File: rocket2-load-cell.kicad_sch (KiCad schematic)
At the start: 34 parts, among them J1 SWD, J2 Screw_Terminal_01x02, Q1 MMBT4403, U2 STM32F103C8Tx, U3 AMS1117-3.3, U4 HX711, Y1 16MHz

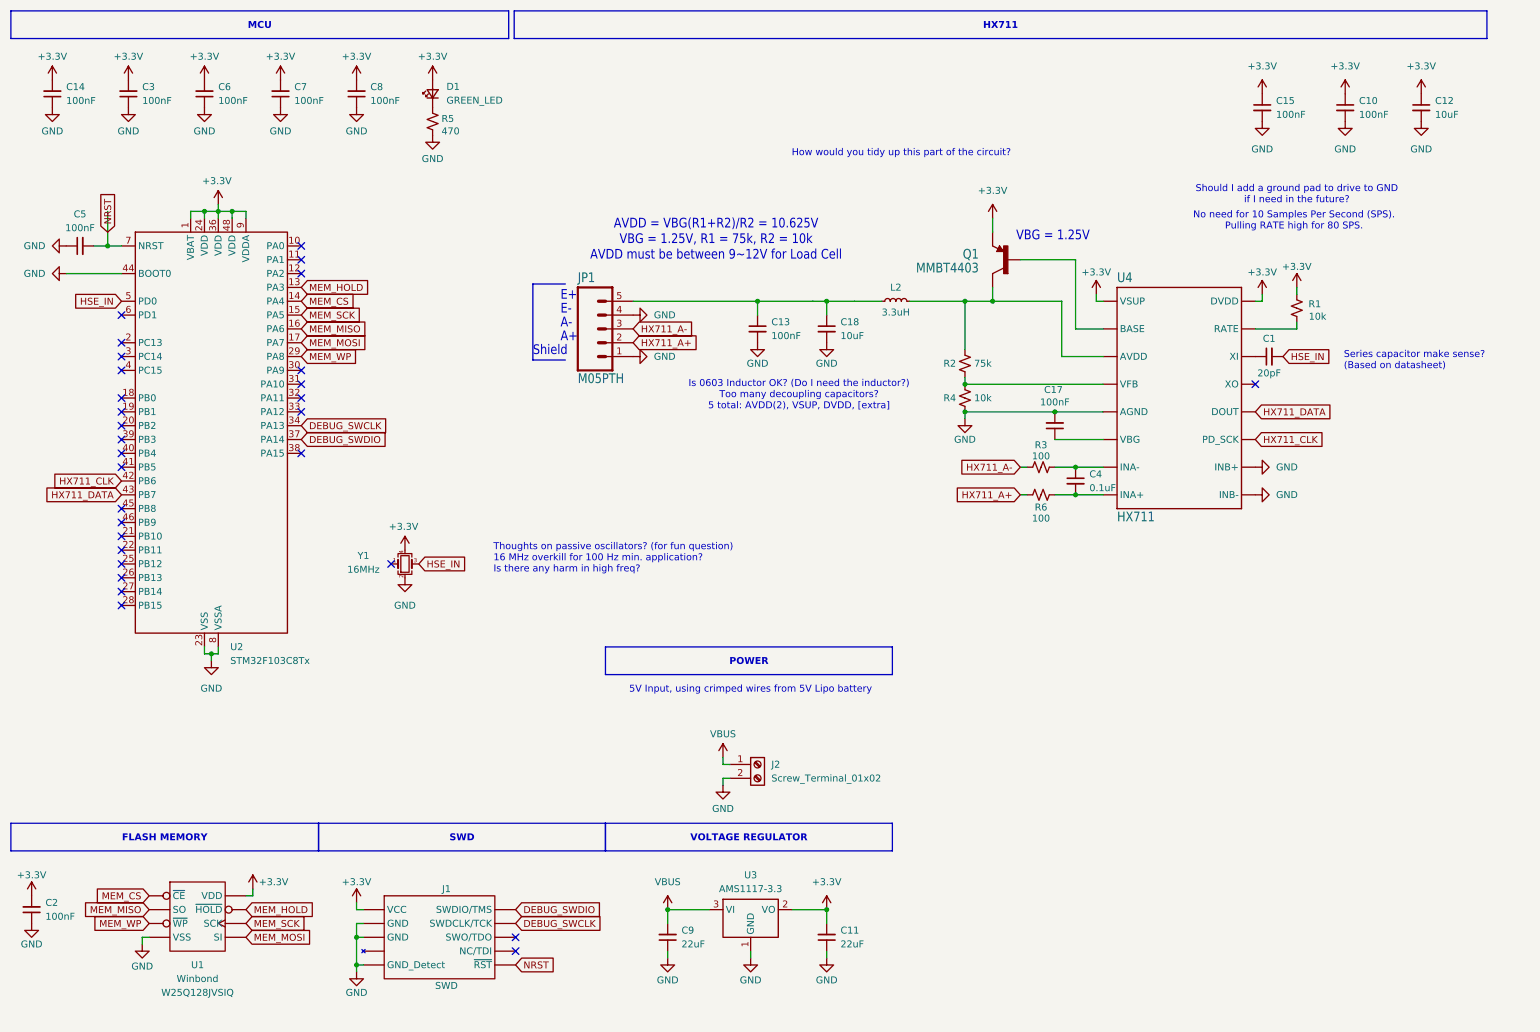
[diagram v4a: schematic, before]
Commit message: Resolved comments. Need new amplifier for faster sampling.
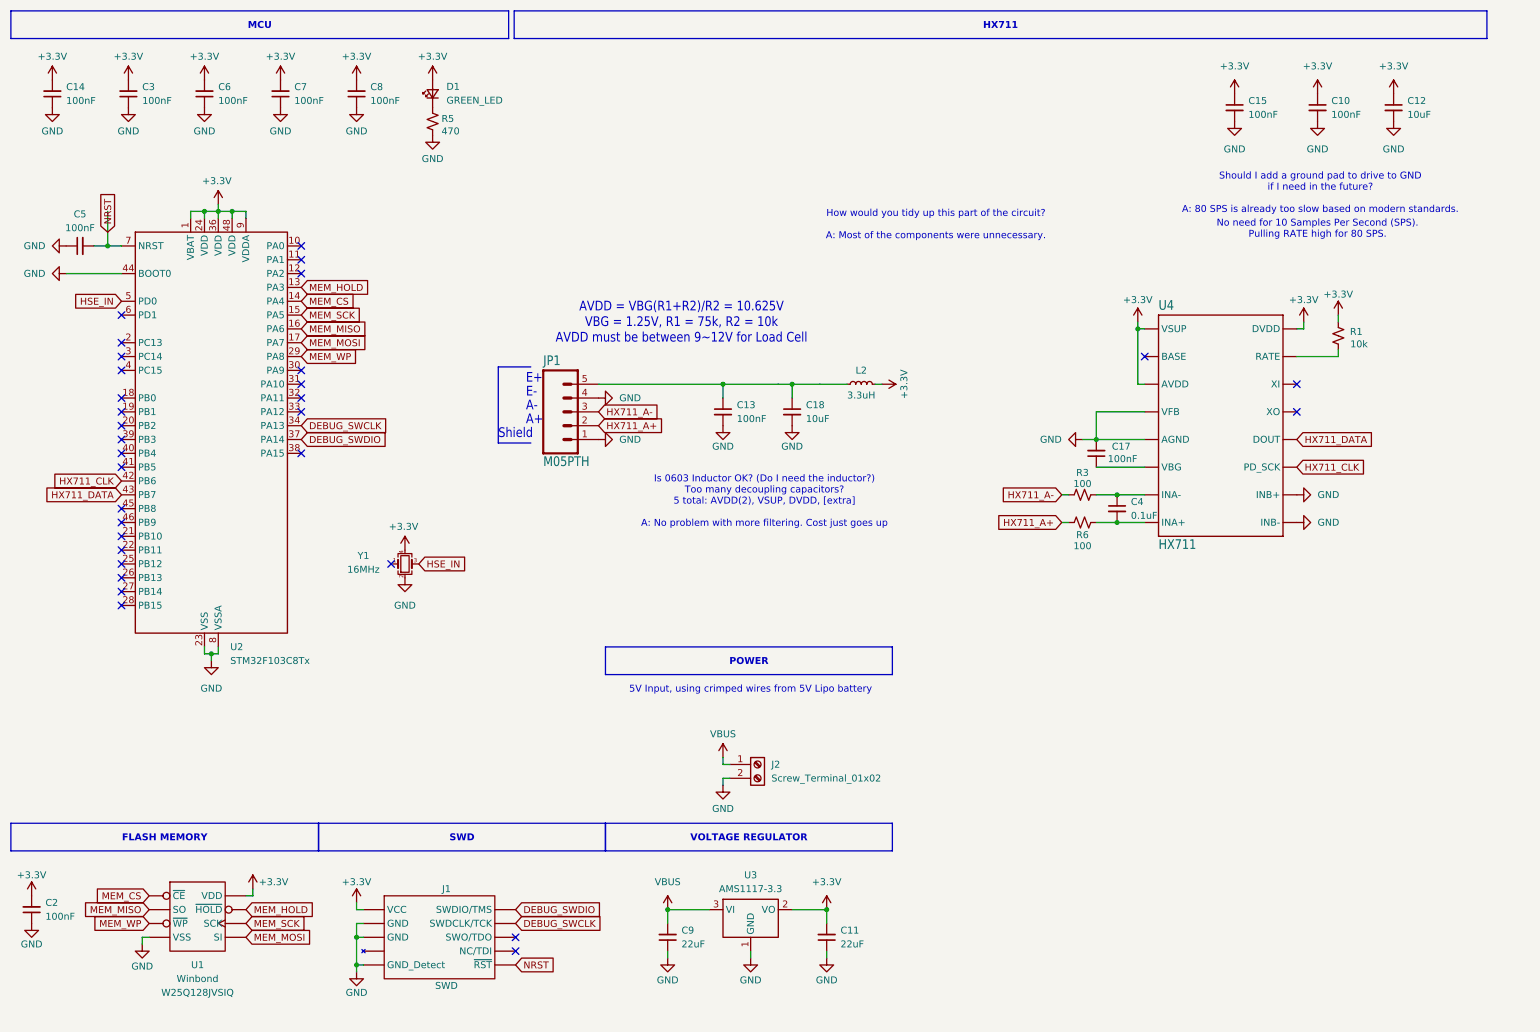
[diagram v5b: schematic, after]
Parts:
- removed C1: 20pF, Capacitor_SMD:C_0603_1608Metric, symbol Device:C_Small
- removed Q1: MMBT4403, symbol SparkFun_HX711_Load_Cell-eagle-import:TRANSISTOR_PNPMMBT4403
- removed R2: 75k, Resistor_SMD:R_0603_1608Metric, symbol Device:R_Small_US
- removed R4: 10k, Resistor_SMD:R_0603_1608Metric, symbol Device:R_Small_US
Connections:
- net +3.3V: now also L2.2, U4.3 (AVDD)
- net GND: now also U4.4 (VFB)
- no-connect marks 30 -> 32
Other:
- note added: "How would you tidy up this part of the circuit? A: Most of the components were unnecessary."
- note added: "Is 0603 Inductor OK? (Do I need the inductor?) Too many decoupling capacitors? 5 total: AVDD(2), VSUP, DVDD, [extra] A: No problem with more filtering. Cost just goes up"
- note added: "Should I add a ground pad to drive to GND if I need in the future? A: 80 SPS is already too slow based on modern standards."
- note removed: "How would you tidy up this part of the circuit?"
- note removed: "Is 0603 Inductor OK? (Do I need the inductor?) Too many decoupling capacitors? 5 total: AVDD(2), VSUP, DVDD, [extra]"
- note removed: "Series capacitor make sense? (Based on datasheet)"
- note removed: "Should I add a ground pad to drive to GND if I need in the future?"
- note removed: "Thoughts on passive oscillators? (for fun question) 16 MHz overkill for 100 Hz min. application? Is there any harm in high freq?"
- note removed: "VBG = 1.25V"
- moved on the sheet: C10, C12, C13, C15, C17, C18, C4, JP1, L2, R1, R3, R6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

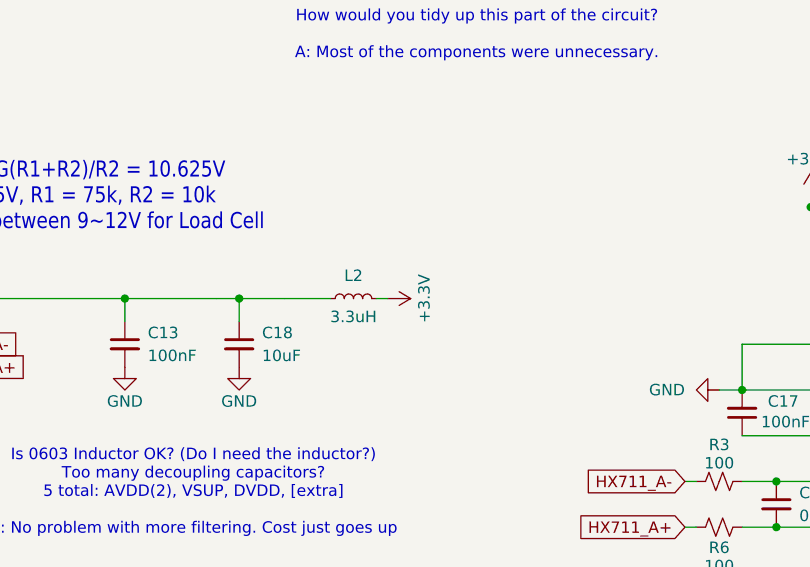
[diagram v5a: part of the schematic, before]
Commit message: Load cell E+ +3.3 -> +5V
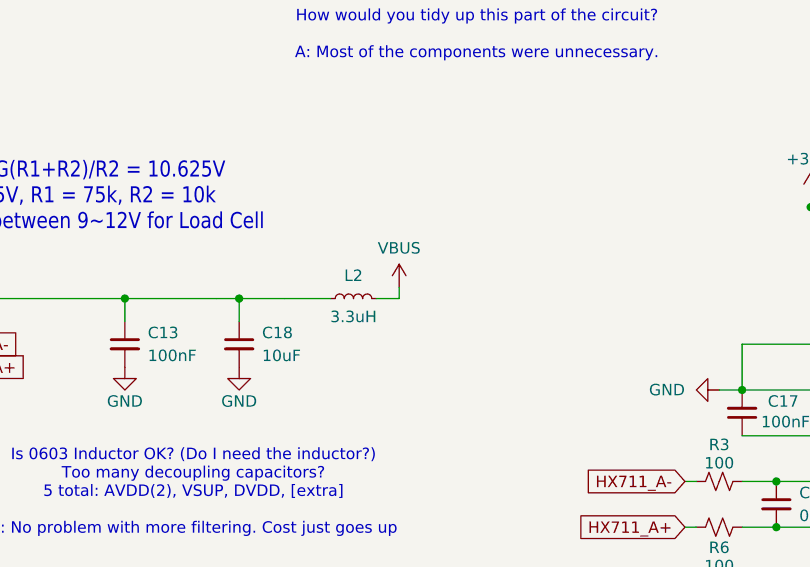
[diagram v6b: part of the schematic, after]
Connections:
- net +3.3V: no longer L2.2
- net VBUS: now also L2.2
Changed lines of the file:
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@@
 	(wire
 		(pts
-			(xy 172.72 81.28) (xy 171.45 81.28)
+			(xy 171.45 81.28) (xy 173.99 81.28)
 		)
 		(stroke
@@
 	(wire
 		(pts
+			(xy 173.99 80.01) (xy 173.99 81.28)
+		)
+		(stroke
+			(width 0)
+			(type default)
+		)
+	)
+	(wire
+		(pts
 			(xy 49.53 130.81) (xy 49.53 132.08)
 		)
@@
 	)
 	(symbol
+		(lib_id "power:VBUS")
+		(at 173.99 80.01 0)
+		(unit 1)
+		(exclude_from_sim no)
+		(in_bom yes)
+		(on_board yes)
+		(dnp no)
+		(property "Reference" "#PWR030"
+			(at 173.99 83.82 0)
+			(effects
+				(font
+					(size 1.27 1.27)
+				)
+				(hide yes)
+			)
+		)
+		(property "Value" "VBUS"
+			(at 173.99 75.692 0)
+			(effects
+				(font
+					(size 1.27 1.27)
+				)
+			)
+		)
+		(property "Footprint" ""
+			(at 173.99 80.01 0)
+			(effects
+				(font
+					(size 1.27 1.27)
+				)
+				(hide yes)
+			)
+		)
+		(property "Datasheet" ""
+			(at 173.99 80.01 0)
+			(effects
+				(font
+					(size 1.27 1.27)
+				)
+				(hide yes)
+			)
+		)
+		(property "Description" "Power symbol creates a global label with name \"VBUS\""
+			(at 173.99 80.01 0)
+			(effects
+				(font
+					(size 1.27 1.27)
+				)
+				(hide yes)
+			)
+		)
+		(pin "1"
+		)
+		(instances
+			(project "rocket2-load-cell"
+				(path "/d1f04dc8-a56c-4379-8ad0-2916e7244fc3"
+					(reference "#PWR030")
+					(unit 1)
+				)
+			)
+		)
+	)
+	(symbol
 		(lib_id "power:GND")
 		(at 266.7 33.02 0)
@@
 					(unit 1)
 				)
-			)
-		)
-	)
-	(symbol
-		(lib_id "power:+3.3V")
-		(at 172.72 81.28 270)
-		(unit 1)
-		(exclude_from_sim no)
-		(in_bom yes)
-		(on_board yes)
-		(dnp no)
-		(property "Reference" "#PWR030"
-			(at 168.91 81.28 0)
-			(effects
-				(font
-					(size 1.27 1.27)
-				)
-				(hide yes)
-			)
-		)
-		(property "Value" "+3.3V"
-			(at 176.784 81.28 0)
-			(effects
-				(font
-					(size 1.27 1.27)
-				)
-			)
-		)
-		(property "Footprint" ""
-			(at 172.72 81.28 0)
-			(effects
-				(font
-					(size 1.27 1.27)
-				)
-				(hide yes)
-			)
-		)
-		(property "Datasheet" ""
-			(at 172.72 81.28 0)
-			(effects
-				(font
-					(size 1.27 1.27)
-				)
-				(hide yes)
-			)
-		)
-		(property "Description" "Power symbol creates a global label with name \"+3.3V\""
-			(at 172.72 81.28 0)
-			(effects
-				(font
-					(size 1.27 1.27)
-				)
-				(hide yes)
-			)
-		)
-		(pin "1"
-		)
-		(instances
-			(project "rocket2-load-cell"
-				(path "/d1f04dc8-a56c-4379-8ad0-2916e7244fc3"
-					(reference "#PWR030")
-					(unit 1)
-				)

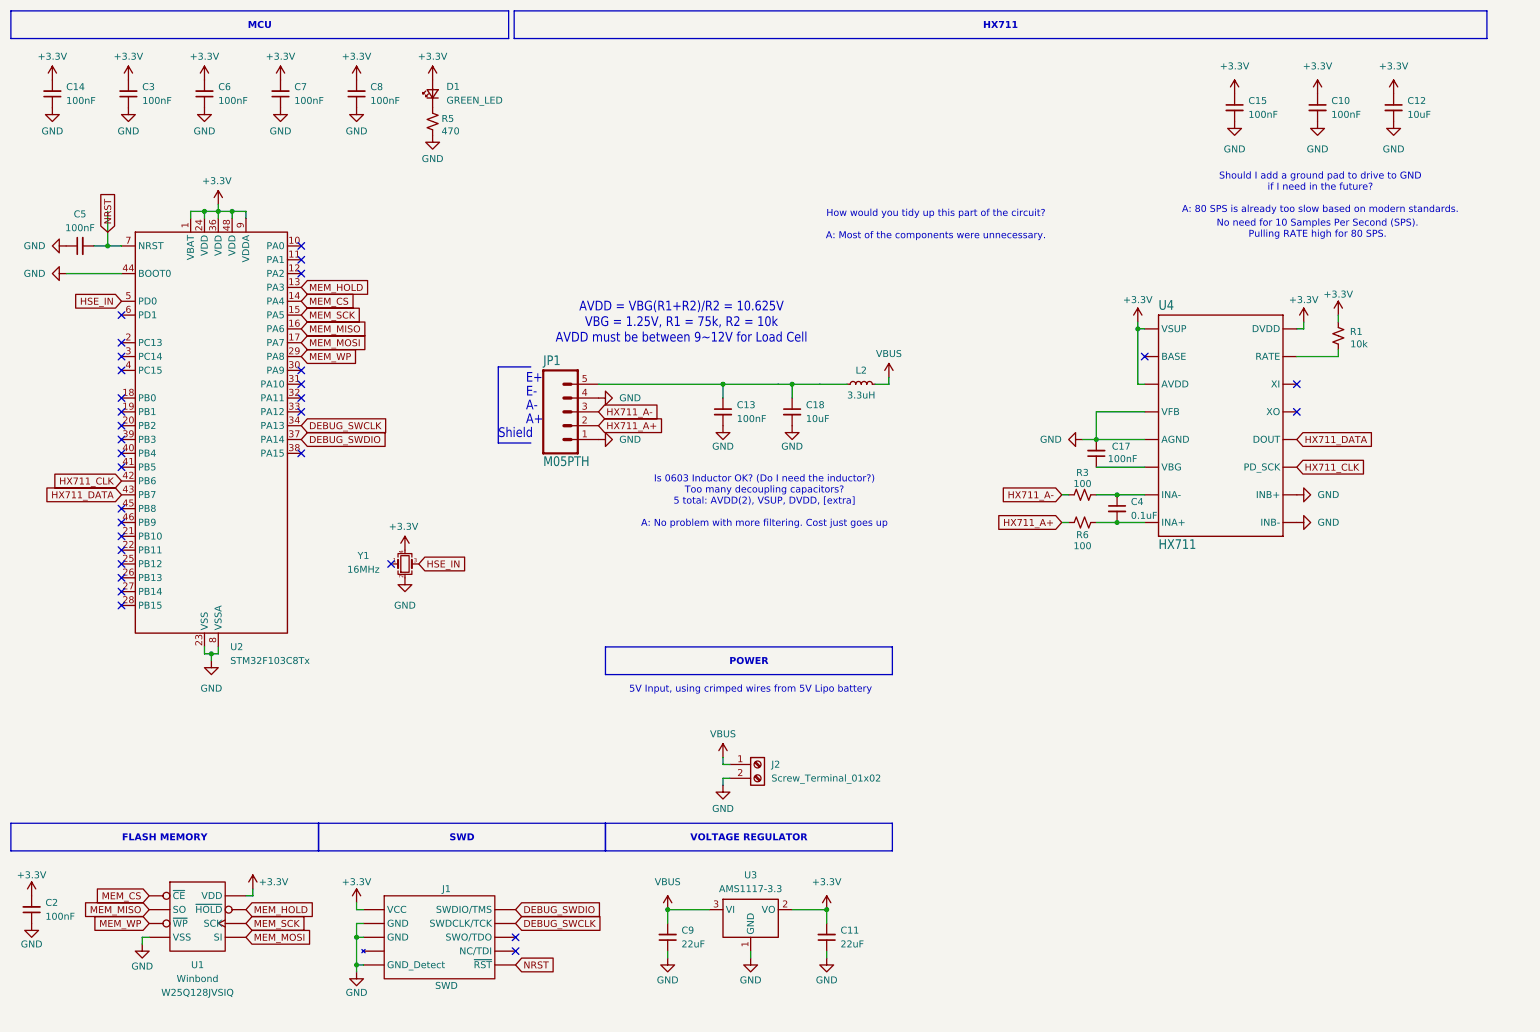
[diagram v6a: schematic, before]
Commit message: added working arduino code as well as testread.py(nonop)
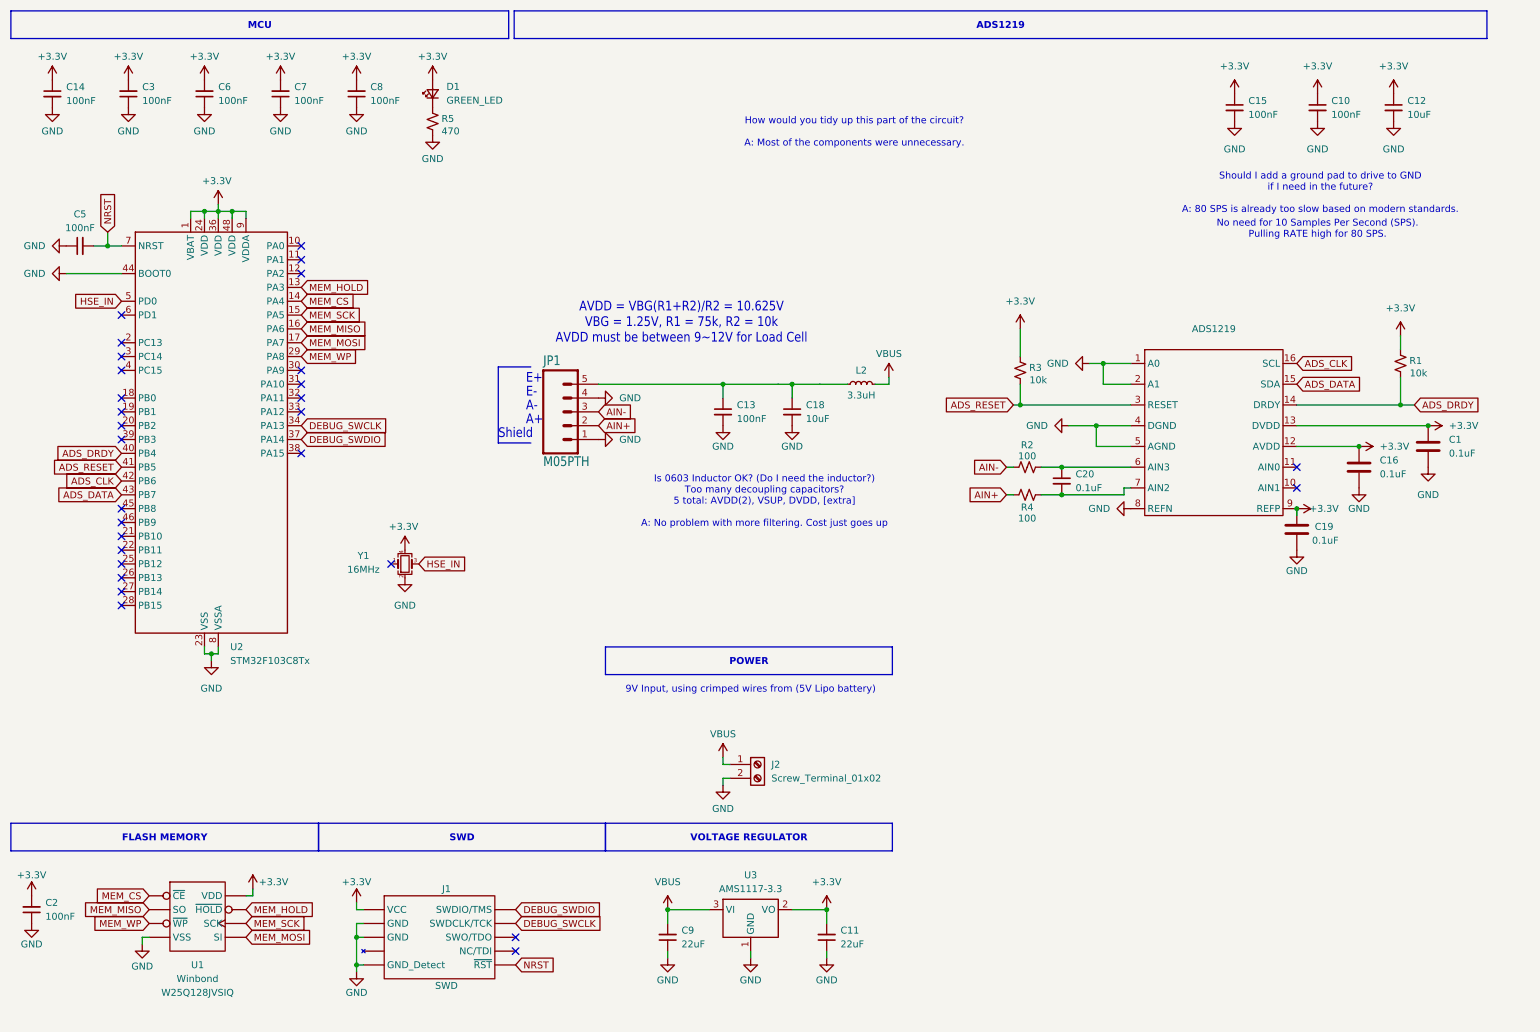
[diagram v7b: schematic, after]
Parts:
- removed C17: 100nF, Capacitor_SMD:C_0603_1608Metric, symbol Device:C_Small
- removed C4: 0.1uF, Capacitor_SMD:C_0603_1608Metric, symbol Device:C_Small
- removed R6: 100, Resistor_SMD:R_0603_1608Metric, symbol Device:R_Small_US
- removed U4: HX711, Package_SO:SOP-16_3.9x9.9mm_P1.27mm, symbol SparkFun_HX711_Load_Cell-eagle-import:HX711HX711
- added ADS1219: ~, Package_SO:TSSOP-16_4.4x5mm_P0.65mm, symbol load-cell-lib:ADS1219
- added C1: 0.1uF, Capacitor_SMD:C_0603_1608Metric, symbol Device:C
- added C16, C19: 0.1uF, Capacitor_SMD:C_0603_1608Metric_Pad1.08x0.95mm_HandSolder, symbol Device:C
- added C20: 0.1uF, Capacitor_SMD:C_0603_1608Metric, symbol Device:C_Small
- added R2, R4: 100, Resistor_SMD:R_0603_1608Metric, symbol Device:R_Small_US
- R3: value 100 -> 10k
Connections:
- net +3.3V: now also C14.1, R3.2, ADS1219.12 (AVDD), ADS1219.13 (DVDD), ADS1219.9 (REFP), C1.1, C16.1, C19.1; no longer C14.2
- net GND: now also C14.2, ADS1219.1 (A0), ADS1219.2 (A1), ADS1219.4 (DGND), ADS1219.5 (AGND), ADS1219.8 (REFN), C1.2, C16.2, C19.2; no longer C14.1
- net ADS_DRDY: now reaches U2.40 (PB4)
- net ADS_DRDY: now also R1.1, ADS1219.14 (DRDY)
- net ADS_RESET: now reaches U2.41 (PB5)
- net ADS_RESET: now also R3.1, ADS1219.3 (RESET)
- net HX711_A+ renamed AIN+
- net AIN+: now also R4.1
- net HX711_A- renamed AIN-
- net AIN-: now also R2.1; no longer R3.1
- net HX711_CLK renamed ADS_CLK
- net ADS_CLK: now also ADS1219.16 (SCL)
- net HX711_DATA renamed ADS_DATA
- net ADS_DATA: now also ADS1219.15 (SDA)
- new net: ADS1219.7 (AIN2), C20.2, R4.2
- new net: ADS1219.6 (AIN3), C20.1, R2.2
- no-connect marks 32 -> 29
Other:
- note added: "9V Input, using crimped wires from (5V Lipo battery)"
- note removed: "5V Input, using crimped wires from 5V Lipo battery"
- moved on the sheet: C14

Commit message: fixed back up issue
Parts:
- removed C10, C15: 100nF, Capacitor_SMD:C_0603_1608Metric, symbol Device:C_Small
- removed C12: 10uF, Capacitor_SMD:C_0603_1608Metric, symbol Device:C_Small
- added H1, H2, H3, H4: MountingHole, MountingHole:MountingHole_3.2mm_M3, symbol Mechanical:MountingHole
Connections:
- net ADS_RESET: no longer ADS1219.3 (RESET), R3.1
- net AIN+: now also JP1.5; no longer JP1.2
- net AIN-: now also JP1.4; no longer JP1.3
- net GND: now also JP1.2; no longer JP1.4
- net at C13.1, C18.1, L2.1: now also JP1.3; no longer JP1.5
- new net: ADS1219.3 (RESET), R3.1
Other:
- note added: "Made to use standard M3 screws"
- moved on the sheet: C13, C18, L2
